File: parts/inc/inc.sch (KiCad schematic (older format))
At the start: 20 parts, among them J1 Conn_02x02_Odd_Even, J2 Conn_02x04_Odd_Even, K1 HK19F

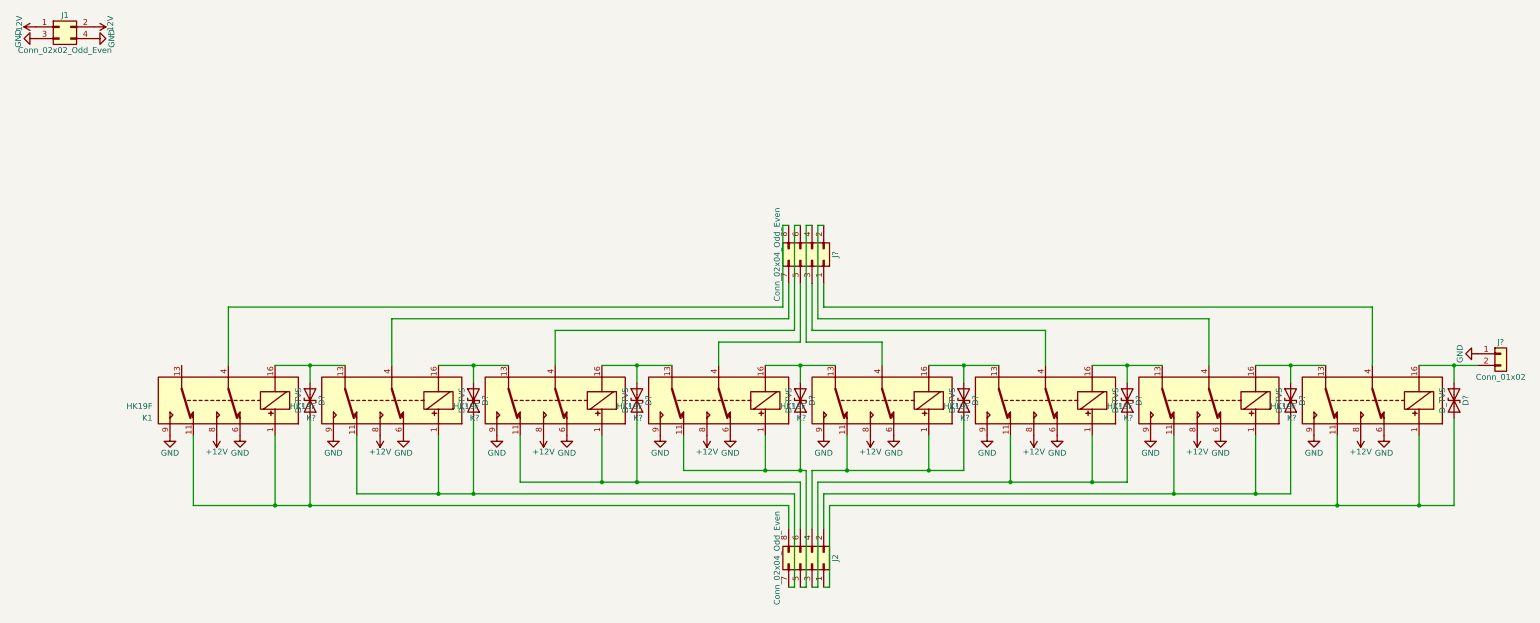
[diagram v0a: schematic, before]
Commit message: Finish inc (now also with carry out).
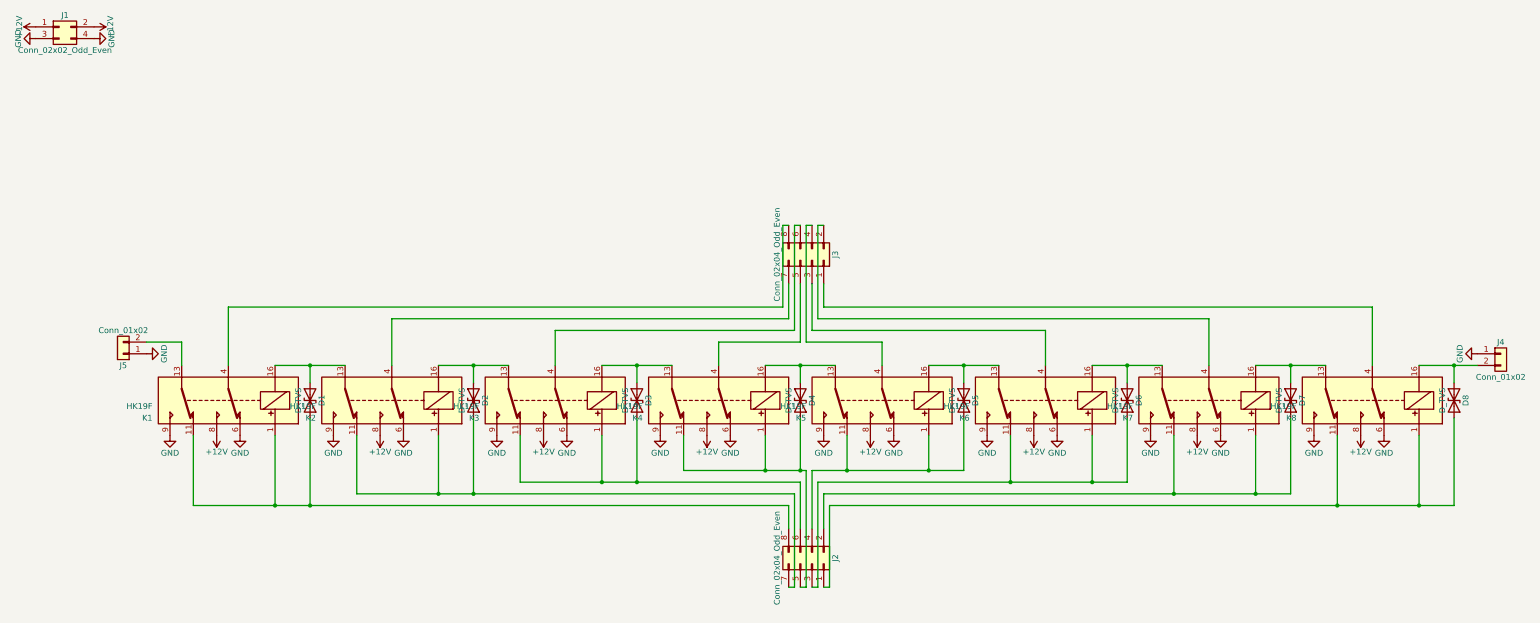
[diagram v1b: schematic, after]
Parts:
- added J5: Conn_01x02, Pin_Headers:Pin_Header_Straight_1x02_Pitch2.54mm, symbol Conn_01x02
- D1, D2, D3, D4, D5, D6, D7, D8: renamed from D?; footprint (none) -> Diodes_SMD:D_2114
- J4: renamed from J?; footprint (none) -> Pin_Headers:Pin_Header_Straight_1x02_Pitch2.54mm
- gave numbers to parts that had none: 8
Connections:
- net GND: now also J5.1 (Pin_1)
- net at K1.13: now also J5.2 (Pin_2)

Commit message: Update to new Kicad, finish reg.
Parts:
- D1, D2, D3, D4, D5, D6, D7, D8: symbol D_TVS -> inc-rescue:D_TVS
- J1: symbol Conn_02x02_Odd_Even -> inc-rescue:Conn_02x02_Odd_Even
- J2, J3: symbol Conn_02x04_Odd_Even -> inc-rescue:Conn_02x04_Odd_Even
- J4, J5: symbol Conn_01x02 -> inc-rescue:Conn_01x02
- K1, K2, K3, K4, K5, K6, K7, K8: symbol HK19F -> inc-rescue:HK19F
